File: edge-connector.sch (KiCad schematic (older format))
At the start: 3 parts

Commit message: Fix USB3300 circuit
-remove 1V8 connection
-add capacitance at internal 1v8 regulators
-apply changes to PCB
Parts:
- J?: footprint artix-dc-scm-footprints:SFF-TA-1002-4C+ -> _autosave-artix-dc-scm-footprints:SFF-TA-1002-4C+; symbol artix-dc-scm:SFF-TA-1002-4C+ -> _autosave-artix-dc-scm:SFF-TA-1002-4C+
- R136, R137: footprint artix-dc-scm-footprints:0402-res -> _autosave-artix-dc-scm-footprints:0402-res; symbol artix-dc-scm:R_0R_0402 -> _autosave-artix-dc-scm:R_0R_0402
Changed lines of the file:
@@
 Connection ~ 6925 10425
 $Comp
-L artix-dc-scm:GND-artix-dc-scm #PWR026
+L _autosave-artix-dc-scm:GND-artix-dc-scm #PWR026
 U 1 1 626F241B
 P 6925 10625
@@
 	8825 10425 8825 10625
 $Comp
-L artix-dc-scm:GND-artix-dc-scm #PWR027
+L _autosave-artix-dc-scm:GND-artix-dc-scm #PWR027
 U 1 1 62BB82B7
 P 8825 10625
@@
 $EndComp
 $Comp
-L artix-dc-scm:R_0R_0402 R136
+L _autosave-artix-dc-scm:R_0R_0402 R136
 U 1 1 616ABCDE
 P 9050 6725
 F 0 "R136" H 9050 6938 60  0000 C CNN
 F 1 "R_0R_0402" H 9050 6575 60  0001 C CNN
-F 2 "artix-dc-scm-footprints:0402-res" H 9250 6925 60  0001 L CNN
+F 2 "_autosave-artix-dc-scm-footprints:0402-res" H 9250 6925 60  0001 L CNN
 F 3 "" H 9050 6725 50  0001 C CNN
 F 4 "PANASONIC" H 9250 7125 60  0001 L CNN "Manufacturer"
@@
 SGPIO0_CLK
 $Comp
-L artix-dc-scm:R_0R_0402 R137
+L _autosave-artix-dc-scm:R_0R_0402 R137
 U 1 1 617019A6
 P 10275 6725
 F 0 "R137" H 10275 6938 60  0000 C CNN
 F 1 "R_0R_0402" H 10275 6575 60  0001 C CNN
-F 2 "artix-dc-scm-footprints:0402-res" H 10475 6925 60  0001 L CNN
+F 2 "_autosave-artix-dc-scm-footprints:0402-res" H 10475 6925 60  0001 L CNN
 F 3 "" H 10275 6725 50  0001 C CNN
 F 4 "PANASONIC" H 10475 7125 60  0001 L CNN "Manufacturer"
@@
 PCIE_HPM_TX[0]_P
 $Comp
-L artix-dc-scm:SFF-TA-1002-4C+ J?
+L _autosave-artix-dc-scm:SFF-TA-1002-4C+ J?
 U 1 1 601205AF
 P 7875 1425
 F 0 "J?" H 7875 1590 50  0000 C CNN
 F 1 "SFF-TA-1002-4C+" H 7875 1499 50  0000 C CNN
-F 2 "artix-dc-scm-footprints:SFF-TA-1002-4C+" H 8025 1475 50  0001 C CNN
+F 2 "_autosave-artix-dc-scm-footprints:SFF-TA-1002-4C+" H 8025 1475 50  0001 C CNN
 F 3 "https://cdn.amphenol-icc.com/media/wysiwyg/files/documentation/sme005.pdf?__cf_chl_jschl_tk__=4604d1306574a1ee474ea914090d3e0c57e266a6-1606907014-0-AbkYBTCTl__kMBcY3BDmgKpfUy32FqitwN2Lniuy8W-uyv2Ev04Q-Q5Mr7srIz_Wnur0_9chB4CRbxKSYcEh7IvAJYsUgJ0PWIS5YdRqqHg567uaZciEX2hQP4ss5l6M4XdNrxEjJppHvyRV3ku89t-VmUSzhgCb8oJlyHpTxST4dEmKZNXfM53TM0tmGirdVbCRt1Byrx5pkz_uMvNABIOj7B2-eDGK52J3DWRD76zEyjdxY7Iz11gPiOY5i_QGIR3uOwkR5LBPNXe8zGqAf8--AKa7RqDbIriQRt90_32C4zIuHqbGa05BXS135E65ov80PbVcb4eSiutCqcJUAacUwu3eVnXVeIumfihJxuP8Rv7_n6saeG_2IuQpEiskzovLGKZM3667Y-rm-AL1NRXTamtvBxqTk0vyMvZ60FgJ" H 8075 1375 50  0001 C CNN
 	1    7875 1425

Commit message: Fixed libs
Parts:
- J?: footprint _autosave-artix-dc-scm-footprints:SFF-TA-1002-4C+ -> artix-dc-scm-footprints:SFF-TA-1002-4C+; symbol _autosave-artix-dc-scm:SFF-TA-1002-4C+ -> artix-dc-scm:SFF-TA-1002-4C+
- R136, R137: footprint _autosave-artix-dc-scm-footprints:0402-res -> artix-dc-scm-footprints:0402-res; symbol _autosave-artix-dc-scm:R_0R_0402 -> artix-dc-scm:R_0R_0402
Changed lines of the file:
@@
 Connection ~ 6925 10425
 $Comp
-L _autosave-artix-dc-scm:GND-artix-dc-scm #PWR026
+L artix-dc-scm:GND-artix-dc-scm #PWR026
 U 1 1 626F241B
 P 6925 10625
@@
 	8825 10425 8825 10625
 $Comp
-L _autosave-artix-dc-scm:GND-artix-dc-scm #PWR027
+L artix-dc-scm:GND-artix-dc-scm #PWR027
 U 1 1 62BB82B7
 P 8825 10625
@@
 $EndComp
 $Comp
-L _autosave-artix-dc-scm:R_0R_0402 R136
+L artix-dc-scm:R_0R_0402 R136
 U 1 1 616ABCDE
 P 9050 6725
 F 0 "R136" H 9050 6938 60  0000 C CNN
 F 1 "R_0R_0402" H 9050 6575 60  0001 C CNN
-F 2 "_autosave-artix-dc-scm-footprints:0402-res" H 9250 6925 60  0001 L CNN
+F 2 "artix-dc-scm-footprints:0402-res" H 9250 6925 60  0001 L CNN
 F 3 "" H 9050 6725 50  0001 C CNN
 F 4 "PANASONIC" H 9250 7125 60  0001 L CNN "Manufacturer"
@@
 SGPIO0_CLK
 $Comp
-L _autosave-artix-dc-scm:R_0R_0402 R137
+L artix-dc-scm:R_0R_0402 R137
 U 1 1 617019A6
 P 10275 6725
 F 0 "R137" H 10275 6938 60  0000 C CNN
 F 1 "R_0R_0402" H 10275 6575 60  0001 C CNN
-F 2 "_autosave-artix-dc-scm-footprints:0402-res" H 10475 6925 60  0001 L CNN
+F 2 "artix-dc-scm-footprints:0402-res" H 10475 6925 60  0001 L CNN
 F 3 "" H 10275 6725 50  0001 C CNN
 F 4 "PANASONIC" H 10475 7125 60  0001 L CNN "Manufacturer"
@@
 PCIE_HPM_TX[0]_P
 $Comp
-L _autosave-artix-dc-scm:SFF-TA-1002-4C+ J?
+L artix-dc-scm:SFF-TA-1002-4C+ J?
 U 1 1 601205AF
 P 7875 1425
 F 0 "J?" H 7875 1590 50  0000 C CNN
 F 1 "SFF-TA-1002-4C+" H 7875 1499 50  0000 C CNN
-F 2 "_autosave-artix-dc-scm-footprints:SFF-TA-1002-4C+" H 8025 1475 50  0001 C CNN
+F 2 "artix-dc-scm-footprints:SFF-TA-1002-4C+" H 8025 1475 50  0001 C CNN
 F 3 "https://cdn.amphenol-icc.com/media/wysiwyg/files/documentation/sme005.pdf?__cf_chl_jschl_tk__=4604d1306574a1ee474ea914090d3e0c57e266a6-1606907014-0-AbkYBTCTl__kMBcY3BDmgKpfUy32FqitwN2Lniuy8W-uyv2Ev04Q-Q5Mr7srIz_Wnur0_9chB4CRbxKSYcEh7IvAJYsUgJ0PWIS5YdRqqHg567uaZciEX2hQP4ss5l6M4XdNrxEjJppHvyRV3ku89t-VmUSzhgCb8oJlyHpTxST4dEmKZNXfM53TM0tmGirdVbCRt1Byrx5pkz_uMvNABIOj7B2-eDGK52J3DWRD76zEyjdxY7Iz11gPiOY5i_QGIR3uOwkR5LBPNXe8zGqAf8--AKa7RqDbIriQRt90_32C4zIuHqbGa05BXS135E65ov80PbVcb4eSiutCqcJUAacUwu3eVnXVeIumfihJxuP8Rv7_n6saeG_2IuQpEiskzovLGKZM3667Y-rm-AL1NRXTamtvBxqTk0vyMvZ60FgJ" H 8075 1375 50  0001 C CNN
 	1    7875 1425

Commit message: update loclib
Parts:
- removed J?: SFF-TA-1002-4C+, artix-dc-scm-footprints:SFF-TA-1002-4C+, symbol artix-dc-scm:SFF-TA-1002-4C+
- added J9: SFF-TA-1002-4C+, artix-dc-scm-footprints:SFF-TA-1002-4C+, symbol artix-dc-scm:SFF-TA-1002-4C+
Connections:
- net 3V0_BAT: now also J9.B41
- net CHASI#: now also J9.A54
- net DBP_PRDY_N: now also J9.A50
- net DBP_PREQ_N: now also J9.A49
- net ESPI_ALERT_N: now also J9.B3
- net ESPI_CLK: now also J9.B1
- net ESPI_CS0_N: now also J9.B2
- net ESPI_CS1_N: now also J9.B9
- net ESPI_IO0: now also J9.B5
- net ESPI_IO1: now also J9.B6
- net ESPI_IO2: now also J9.B7
- net ESPI_IO3: now also J9.B8
- net ESPI_RESET_N: now also J9.B4
- net GND: now also J9.A11 (GND), J9.A14 (GND), J9.A17 (GND), J9.A20 (GND), J9.A33 (GND), J9.A42 (GND), J9.A58 (GND), J9.A61 (GND), J9.A64 (GND), J9.A67 (GND), J9.A70 (GND), J9.B10 (GND), J9.B17 (GND), J9.B26 (GND), J9.B33 (GND), J9.B38 (GND), J9.B49 (GND), J9.B52 (GND), J9.B55 (GND), J9.B58 (GND), J9.B61 (GND), J9.B64 (GND), J9.B67 (GND), J9.B70 (GND), J9.OA13 (GND), J9.OA3 (GND), J9.OA4 (GND), J9.OB10 (GND), J9.OB4 (GND), J9.OB7 (GND)
- net HPM_FW_RECOVERY: now also J9.A43
- net HPM_STBY_EN: now also J9.A45
- net HPM_STBY_RDY: now also J9.A44
- net HPM_STBY_RST_N: now also J9.A46
- net I2C[0]_SCL: now also J9.A1
- net I2C[0]_SDA: now also J9.A2
- net I2C[10]_SCL: now also J9.A31
- net I2C[10]_SDA: now also J9.A32
- net I2C[11]_SCL: now also J9.A38
- net I2C[11]_SDA: now also J9.A39
- net I2C[12]_SCL: now also J9.A40
- net I2C[12]_SDA: now also J9.A41
- net I2C[1]_SCL: now also J9.A3
- net I2C[1]_SDA: now also J9.A4
- net I2C[2]_SCL: now also J9.A5
- net I2C[2]_SDA: now also J9.A6
- net I2C[3]_SCL: now also J9.A7
- net I2C[3]_SDA: now also J9.A8
- net I2C[4]_SCL: now also J9.A9
- net I2C[4]_SDA: now also J9.A10
- net I2C[5]_SCL: now also J9.A21
- net I2C[5]_SDA: now also J9.A22
- net I2C[6]_SCL: now also J9.A23
- net I2C[6]_SDA: now also J9.A24
- net I2C[7]_SCL: now also J9.A25
- net I2C[7]_SDA: now also J9.A26
- net I2C[8]_SCL: now also J9.A27
- net I2C[8]_SDA: now also J9.A28
- net I2C[9]_SCL: now also J9.A29
- net I2C[9]_SDA: now also J9.A30
- net I3C[0]_SCL: now also J9.OA5
- net I3C[0]_SDA: now also J9.OA6
- net I3C[1]_SCL: now also J9.OA7
- net I3C[1]_SDA: now also J9.OA8
- net I3C[2]_SCL: now also J9.OA9
- net I3C[2]_SDA: now also J9.OA10
- net I3C[3]_SCL: now also J9.OA11
- net I3C[3]_SDA: now also J9.OA12
- net IRQ_N: now also J9.A56
- net JTAG_TCK: now also J9.A34
- net JTAG_TDI: now also J9.A36
- net JTAG_TDO: now also J9.A37
- net JTAG_TMS: now also J9.A35
- net NCSI_CLK: now also J9.B18
- net NCSI_CRS_DV: now also J9.B19
- net NCSI_RXD0: now also J9.B24
- net NCSI_RXD1: now also J9.B25
- net NCSI_RXER: now also J9.B23
- net NCSI_TXD0: now also J9.B21
- net NCSI_TXD1: now also J9.B22
- net NCSI_TXEN: now also J9.B20
- net P12V_AUX: now also J9.OA1 (P12V_AUX), J9.OA2 (P12V_AUX), J9.OB1 (P12V_AUX), J9.OB2 (P12V_AUX)
- net PCIE_BMC_CLK_100_N: now also J9.A13
- net PCIE_BMC_CLK_100_P: now also J9.A12
- net PCIE_BMC_RX_N: now also J9.A19
- net PCIE_BMC_RX_P: now also J9.A18
- net PCIE_BMC_TX_N: now also J9.A16
- net PCIE_BMC_TX_P: now also J9.A15
- net PCIE_HPM_CLK_N: now also J9.B57
- net PCIE_HPM_CLK_P: now also J9.B56
- net PCIE_HPM_RX[0]_N: now also J9.A60
- net PCIE_HPM_RX[0]_P: now also J9.A59
- net PCIE_HPM_RX[1]_N: now also J9.A63
- net PCIE_HPM_RX[1]_P: now also J9.A62
- net PCIE_HPM_RX[2]_N: now also J9.A66
- net PCIE_HPM_RX[2]_P: now also J9.A65
- net PCIE_HPM_RX[3]_N: now also J9.A69
- net PCIE_HPM_RX[3]_P: now also J9.A68
- net PCIE_HPM_TX[0]_N: now also J9.B60
- net PCIE_HPM_TX[0]_P: now also J9.B59
- net PCIE_HPM_TX[1]_N: now also J9.B63
- net PCIE_HPM_TX[1]_P: now also J9.B62
- net PCIE_HPM_TX[2]_N: now also J9.B66
- net PCIE_HPM_TX[2]_P: now also J9.B65
- net PCIE_HPM_TX[3]_N: now also J9.B69
- net PCIE_HPM_TX[3]_P: now also J9.B68
- net PECI_BMC: now also J9.B27
- net PRSNT0_N: now also J9.OB3
- net PRSNT1_N: now also J9.A57
- net PVCCIO_PECI: now also J9.B28
- net QSPI0_CLK: now also J9.B11
- net QSPI0_CS0_N: now also J9.B12
- net QSPI0_CS1_N: now also J9.B42
- net QSPI0_D0: now also J9.B13
- net QSPI0_D1: now also J9.B14
- net QSPI0_D2: now also J9.B15
- net QSPI0_D3: now also J9.B16
- net QSPI1_CLK: now also J9.B43
- net QSPI1_CS0_N: now also J9.B44
- net QSPI1_D0: now also J9.B45
- net QSPI1_D1: now also J9.B46
- net QSPI1_D2: now also J9.B47
- net QSPI1_D3: now also J9.B48
- net RST_PLTRST_BUF_N: now also J9.A51
- net RoT_CPU_RST_N: now also J9.A53
- net SGPIO0_CLK: now also J9.B30
- net SGPIO0_DI: now also J9.B31
- net SGPIO0_DO: now also J9.B29
- net SGPIO0_LD: now also J9.B32
- net SGPIO1_DI: now also J9.B36
- net SGPIO1_DO: now also J9.B34
- net SGPIO1_LD: now also J9.B37
- net SGPIO_INTR_N: now also J9.B40
- net SGPIO_RESET_N: now also J9.B39
- net SPARE0: now also J9.A55
- net SPARE1: now also J9.A52
- net SPI0_CLK: now also J9.OB11
- net SPI0_CS_N: now also J9.OB12
- net SPI0_MISO: now also J9.OB14
- net SPI0_MOSI: now also J9.OB13
- net SYS_PWRBTN_N: now also J9.A47
- net SYS_PWROK: now also J9.A48
- net UART0_SCM_RX: now also J9.OB9
- net UART0_SCM_TX: now also J9.OB8
- net UART1_SCM_RX: now also J9.OB6
- net UART1_SCM_TX: now also J9.OB5
- net USB1_D_N: now also J9.B54
- net USB1_D_P: now also J9.B53
- net USB2_D_N: now also J9.B51
- net USB2_D_P: now also J9.B50
- net VIRTUAL_RESEAT: now also J9.OA14
- net at R136.1: now also J9.B35
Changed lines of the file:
@@
 PCIE_HPM_TX[0]_P
 $Comp
-L artix-dc-scm:SFF-TA-1002-4C+ J?
-U 1 1 601205AF
+L artix-dc-scm:SFF-TA-1002-4C+ J9
+U 1 1 6012802C
 P 7875 1425
-F 0 "J?" H 7875 1590 50  0000 C CNN
+F 0 "J9" H 7875 1590 50  0000 C CNN
 F 1 "SFF-TA-1002-4C+" H 7875 1499 50  0000 C CNN
 F 2 "artix-dc-scm-footprints:SFF-TA-1002-4C+" H 8025 1475 50  0001 C CNN

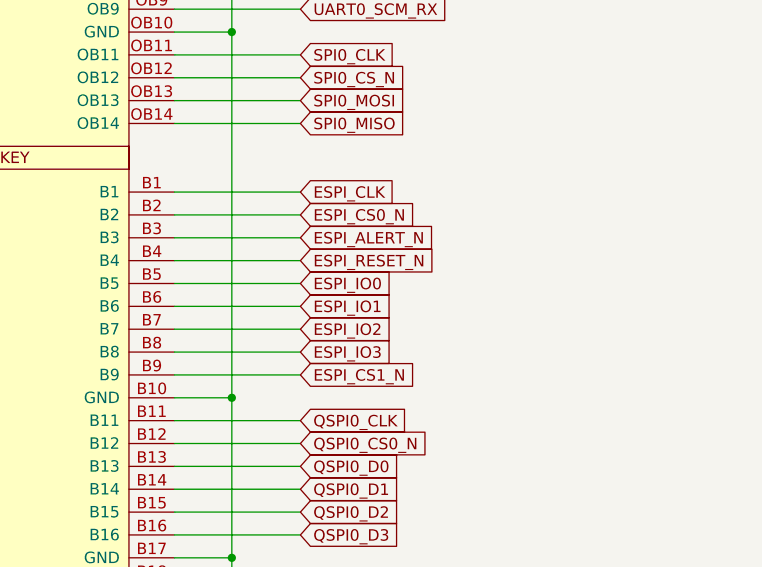
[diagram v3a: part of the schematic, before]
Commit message: Added ESPI level translator
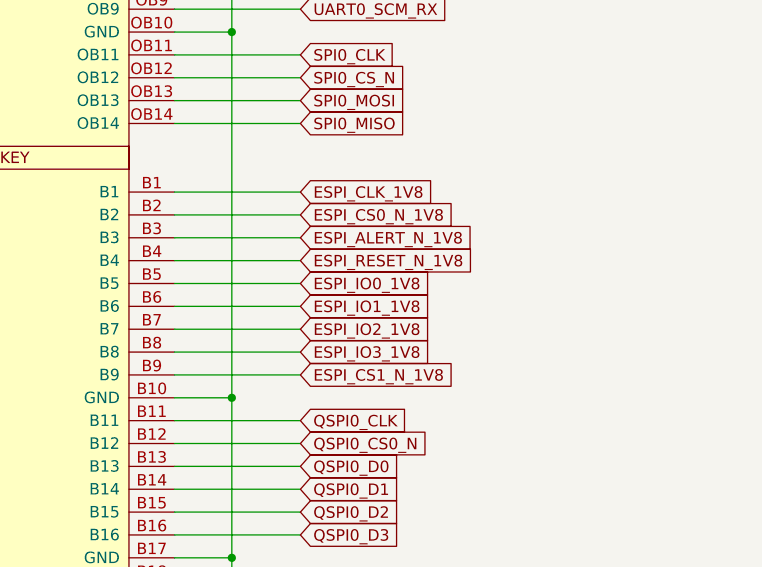
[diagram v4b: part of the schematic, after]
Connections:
- net ESPI_ALERT_N renamed ESPI_ALERT_N_1V8
- net ESPI_CLK renamed ESPI_CLK_1V8
- net ESPI_CS0_N renamed ESPI_CS0_N_1V8
- net ESPI_CS1_N renamed ESPI_CS1_N_1V8
- net ESPI_IO0 renamed ESPI_IO0_1V8
- net ESPI_IO1 renamed ESPI_IO1_1V8
- net ESPI_IO2 renamed ESPI_IO2_1V8
- net ESPI_IO3 renamed ESPI_IO3_1V8
- net ESPI_RESET_N renamed ESPI_RESET_N_1V8
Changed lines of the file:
@@
 Text GLabel 9125 2825 2    50   Input ~ 0
 SPI0_MISO
-Text GLabel 9125 3125 2    50   Input ~ 0
-ESPI_CLK
-Text GLabel 9125 3225 2    50   Input ~ 0
-ESPI_CS0_N
-Text GLabel 9125 3325 2    50   Input ~ 0
-ESPI_ALERT_N
-Text GLabel 9125 3425 2    50   Input ~ 0
-ESPI_RESET_N
-Text GLabel 9125 3525 2    50   Input ~ 0
-ESPI_IO0
-Text GLabel 9125 3625 2    50   Input ~ 0
-ESPI_IO1
-Text GLabel 9125 3725 2    50   Input ~ 0
-ESPI_IO2
-Text GLabel 9125 3825 2    50   Input ~ 0
-ESPI_IO3
-Text GLabel 9125 3925 2    50   Input ~ 0
-ESPI_CS1_N
 Text GLabel 9125 4125 2    50   Input ~ 0
 QSPI0_CLK
@@
 	1    0    0    -1
 $EndComp
+Text GLabel 9125 3525 2    50   Input ~ 0
+ESPI_IO0_1V8
+Text GLabel 9125 3625 2    50   Input ~ 0
+ESPI_IO1_1V8
+Text GLabel 9125 3725 2    50   Input ~ 0
+ESPI_IO2_1V8
+Text GLabel 9125 3825 2    50   Input ~ 0
+ESPI_IO3_1V8
+Text GLabel 9125 3425 2    50   Input ~ 0
+ESPI_RESET_N_1V8
+Text GLabel 9125 3325 2    50   Input ~ 0
+ESPI_ALERT_N_1V8
+Text GLabel 9125 3225 2    50   Input ~ 0
+ESPI_CS0_N_1V8
+Text GLabel 9125 3125 2    50   Input ~ 0
+ESPI_CLK_1V8
+Text GLabel 9125 3925 2    50   Input ~ 0
+ESPI_CS1_N_1V8
 $EndSCHEMATC

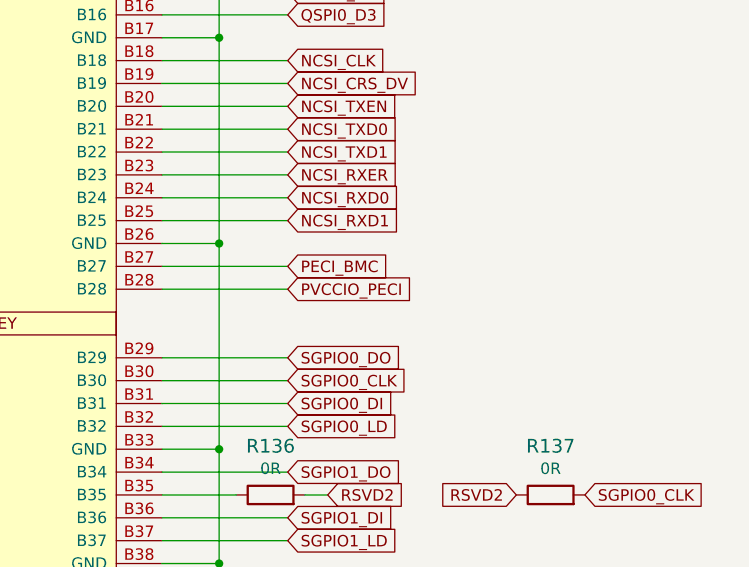
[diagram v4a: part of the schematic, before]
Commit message: Route orphaned signals
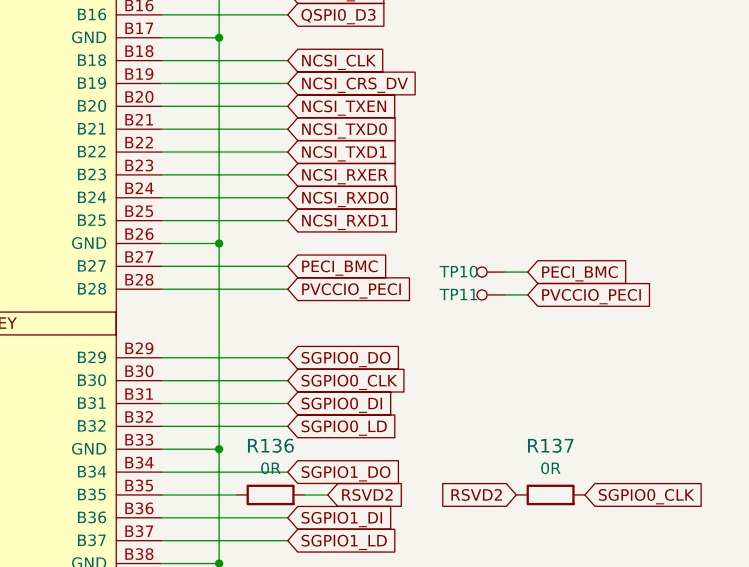
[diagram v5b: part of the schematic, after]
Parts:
- added TP10, TP11: TP_SMD1MM, artix-dc-scm-footprints:Testpoint_smd_1mm, symbol artix-dc-scm:TP_SMD1MM
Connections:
- net PECI_BMC: now also TP10.1
- net PVCCIO_PECI: now also TP11.1
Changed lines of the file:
@@
 	8575 5625 8825 5625
-Wire Wire Line
-	9125 5725 8575 5725
-Wire Wire Line
-	9125 5825 8575 5825
 Wire Wire Line
 	7175 3125 6625 3125
@@
 Text GLabel 9125 3925 2    50   Input ~ 0
 ESPI_CS1_N_1V8
+$Comp
+L artix-dc-scm:TP_SMD1MM TP10
+U 1 1 60D49F2E
+P 9975 5750
+F 0 "TP10" V 9975 5650 50  0000 C CNN
+F 1 "TP_SMD1MM" H 9975 5650 50  0001 C CNN
+F 2 "artix-dc-scm-footprints:Testpoint_smd_1mm" H 10175 5950 60  0001 L CNN
+F 3 "" H 10175 6050 60  0001 L CNN
+	1    9975 5750
+	0    1    1    0
+$EndComp
+$Comp
+L artix-dc-scm:TP_SMD1MM TP11
+U 1 1 60D4A897
+P 9975 5850
+F 0 "TP11" V 9975 5750 50  0000 C CNN
+F 1 "TP_SMD1MM" H 9975 5750 50  0001 C CNN
+F 2 "artix-dc-scm-footprints:Testpoint_smd_1mm" H 10175 6050 60  0001 L CNN
+F 3 "" H 10175 6150 60  0001 L CNN
+	1    9975 5850
+	0    1    1    0
+$EndComp
+Text GLabel 10175 5750 2    50   Input ~ 0
+PECI_BMC
+Text GLabel 10175 5850 2    50   Input ~ 0
+PVCCIO_PECI
+Wire Wire Line
+	8575 5725 9125 5725
+Wire Wire Line
+	8575 5825 9125 5825
+Wire Wire Line
+	10075 5750 10175 5750
+Wire Wire Line
+	10175 5850 10075 5850
 $EndSCHEMATC
